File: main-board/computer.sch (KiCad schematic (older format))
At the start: 18 parts, among them J1 Expansion, J2 Expansion, SW1 RESET, U1 W65C02SxP, U2 28C256, U3 AS6C62256, U4 74HC30, U5 74HC00, U6 DS1813, X1 1MHz

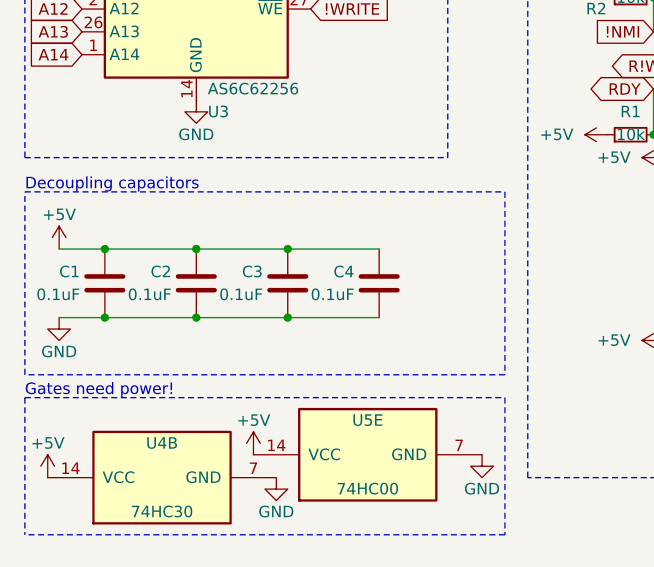
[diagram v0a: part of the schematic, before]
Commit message: Redesign CPU and IO boards
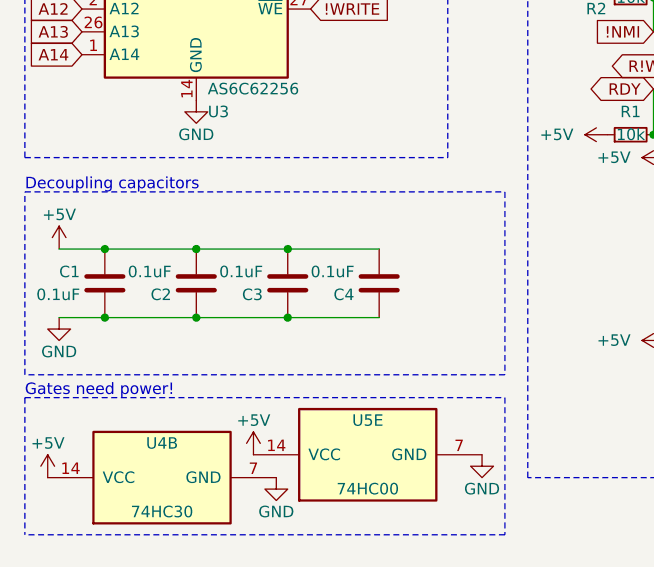
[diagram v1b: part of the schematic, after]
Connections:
- net +5V: now also C2.2, C3.2, C4.2; no longer C2.1, C3.1, C4.1
- net GND: now also C2.1, C3.1, C4.1; no longer C2.2, C3.2, C4.2
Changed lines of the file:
@@
 F 3 "~" H 1750 4700 50  0001 C CNN
 	1    1750 4700
-	1    0    0    -1
+	1    0    0    1
 $EndComp
 $Comp
@@
 F 3 "~" H 1350 4700 50  0001 C CNN
 	1    1350 4700
-	1    0    0    -1
+	1    0    0    1
 $EndComp
 $Comp
@@
 F 3 "~" H 2150 4700 50  0001 C CNN
 	1    2150 4700
-	1    0    0    -1
+	1    0    0    1
 $EndComp
 Text GLabel 7400 4850 0    50   Input ~ 0

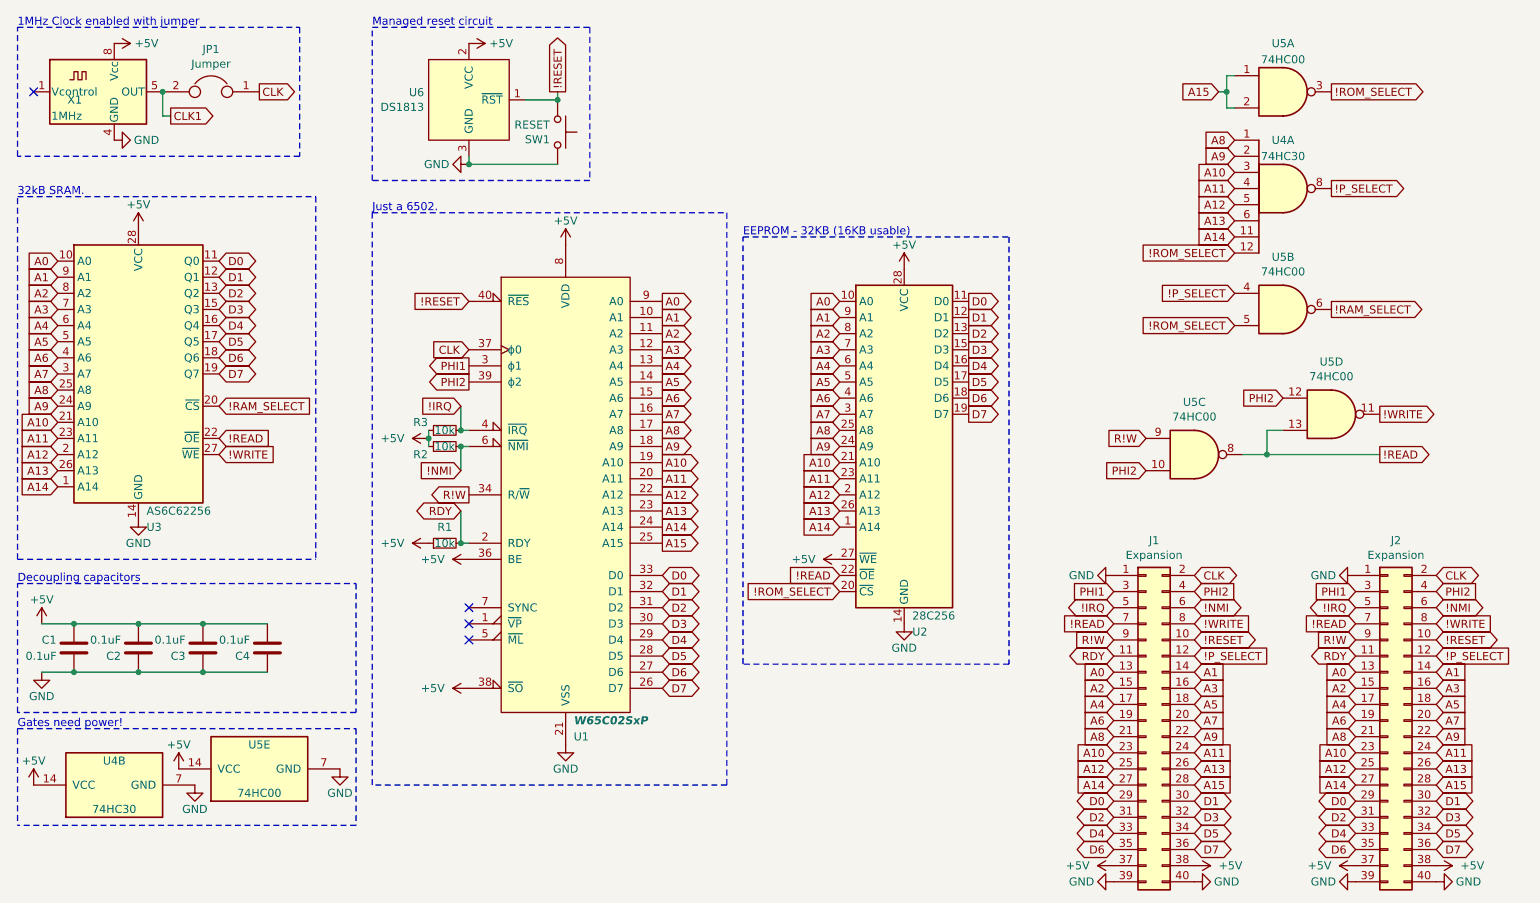
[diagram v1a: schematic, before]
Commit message: Finish designing and routing new CPU and IO boards
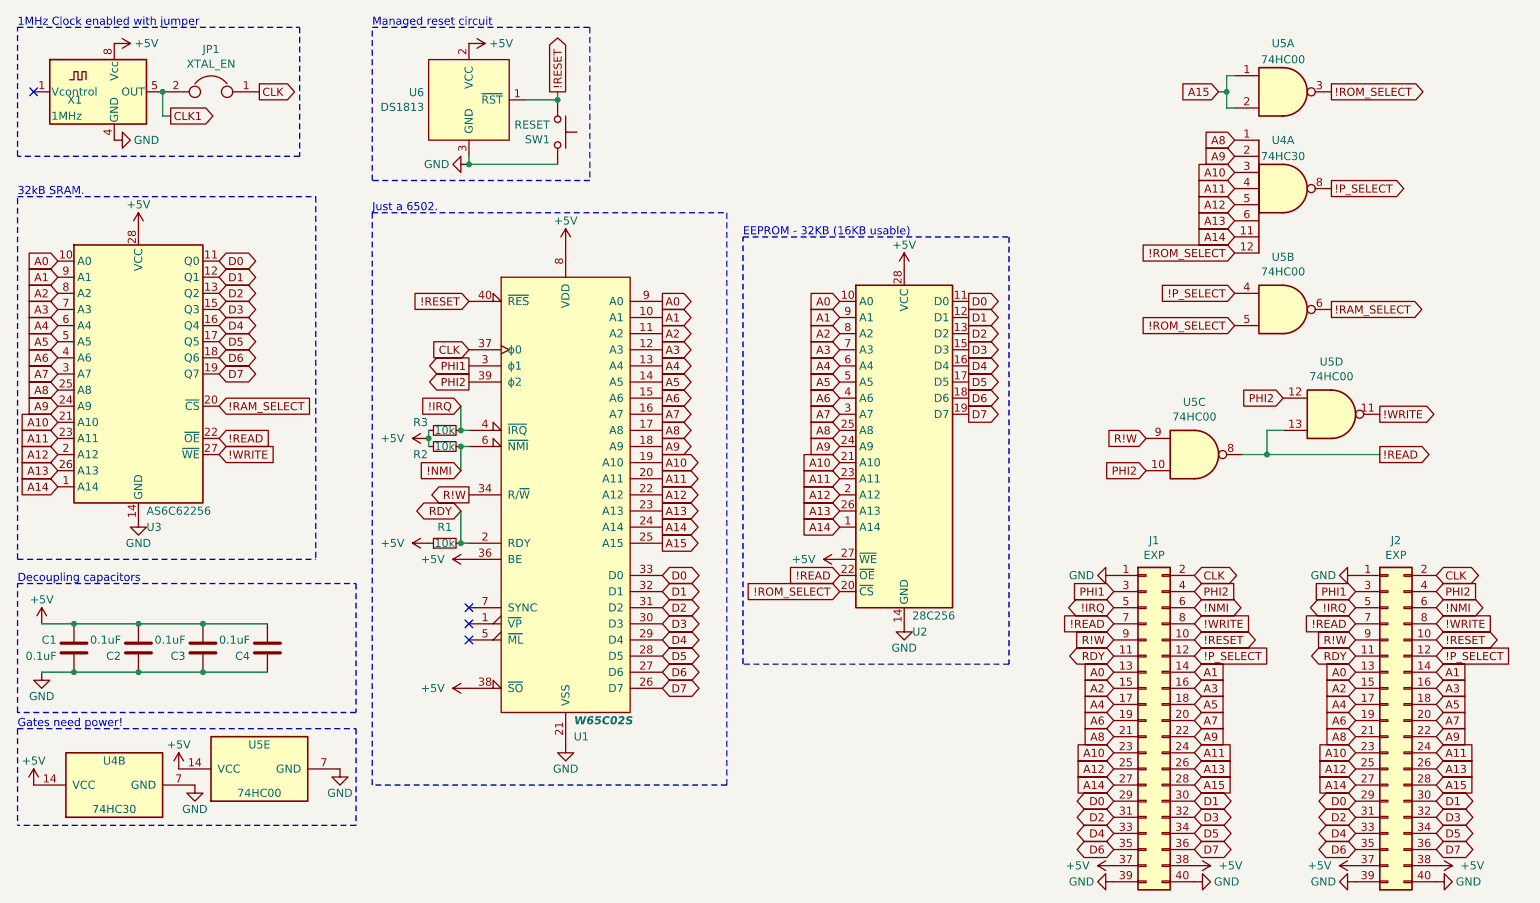
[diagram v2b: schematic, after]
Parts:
- J1, J2: value Expansion -> EXP
- JP1: value Jumper -> XTAL_EN
- U1: value W65C02SxP -> W65C02S
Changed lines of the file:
@@
 P 7600 5150
 F 0 "J1" H 7650 6267 50  0000 C CNN
-F 1 "Expansion" H 7650 6176 50  0000 C CNN
+F 1 "EXP" H 7650 6176 50  0000 C CNN
 F 2 "Connector_PinHeader_2.54mm:PinHeader_2x20_P2.54mm_Vertical" H 7600 5150 50  0001 C CNN
 F 3 "~" H 7600 5150 50  0001 C CNN
@@
 P 1800 1250
 F 0 "JP1" H 1800 1514 50  0000 C CNN
-F 1 "Jumper" H 1800 1423 50  0000 C CNN
+F 1 "XTAL_EN" H 1800 1423 50  0000 C CNN
 F 2 "Connector_PinHeader_2.54mm:PinHeader_1x02_P2.54mm_Horizontal" H 1800 1250 50  0001 C CNN
 F 3 "~" H 1800 1250 50  0001 C CNN
@@
 P 9100 5150
 F 0 "J2" H 9150 6267 50  0000 C CNN
-F 1 "Expansion" H 9150 6176 50  0000 C CNN
+F 1 "EXP" H 9150 6176 50  0000 C CNN
 F 2 "Connector_PinHeader_2.54mm:PinHeader_2x20_P2.54mm_Vertical" H 9100 5150 50  0001 C CNN
 F 3 "~" H 9100 5150 50  0001 C CNN
@@
 P 4000 3750
 F 0 "U1" H 4050 2250 50  0000 L CNN
-F 1 "W65C02SxP" H 4050 2350 50  0000 L CIB
+F 1 "W65C02S" H 4050 2350 50  0000 L CIB
 F 2 "Package_DIP:DIP-40_W15.24mm_Socket" H 4000 5750 50  0001 C CNN
 F 3 "http://www.westerndesigncenter.com/wdc/documentation/w65c02s.pdf" H 4000 5650 50  0001 C CNN
